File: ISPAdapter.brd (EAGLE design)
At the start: 76 x 38 mm, 10 parts, among them U1 74LVC4066PW

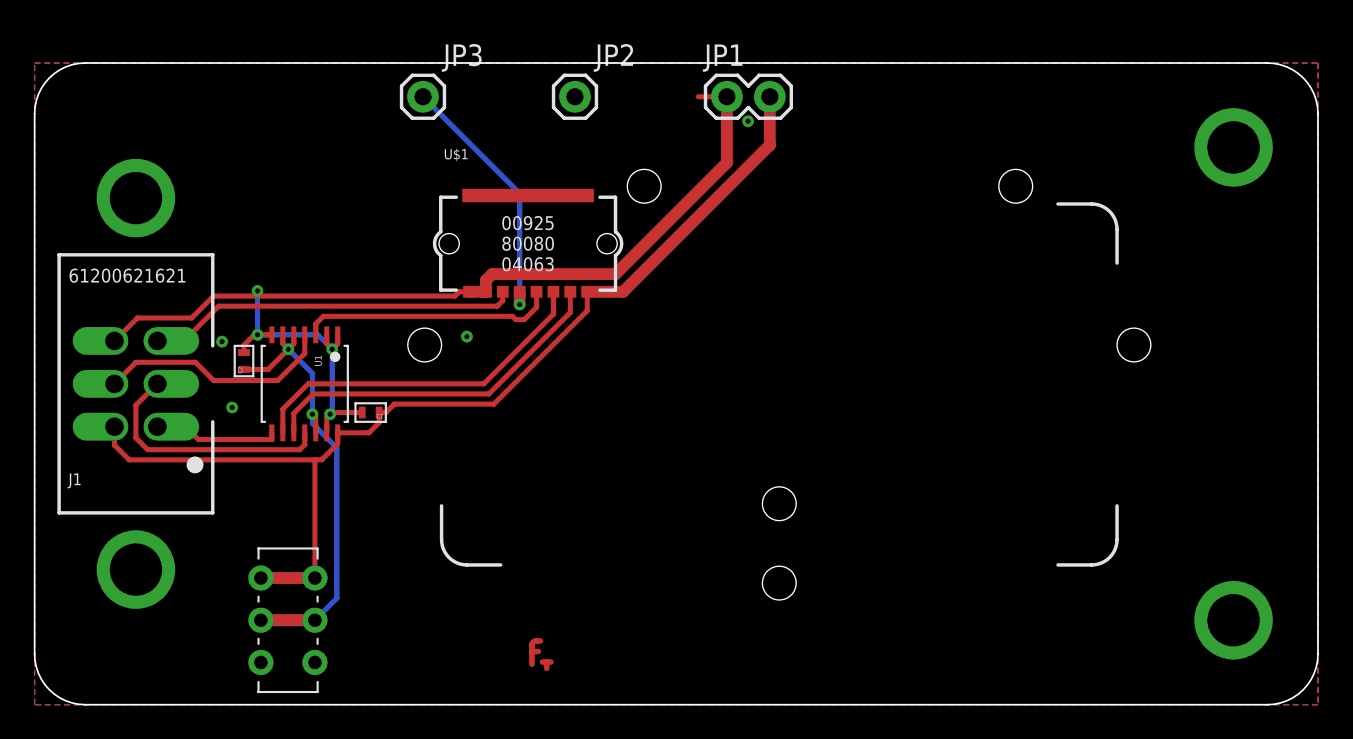
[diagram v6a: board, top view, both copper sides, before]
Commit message: Jack/Plug refs; offset pads
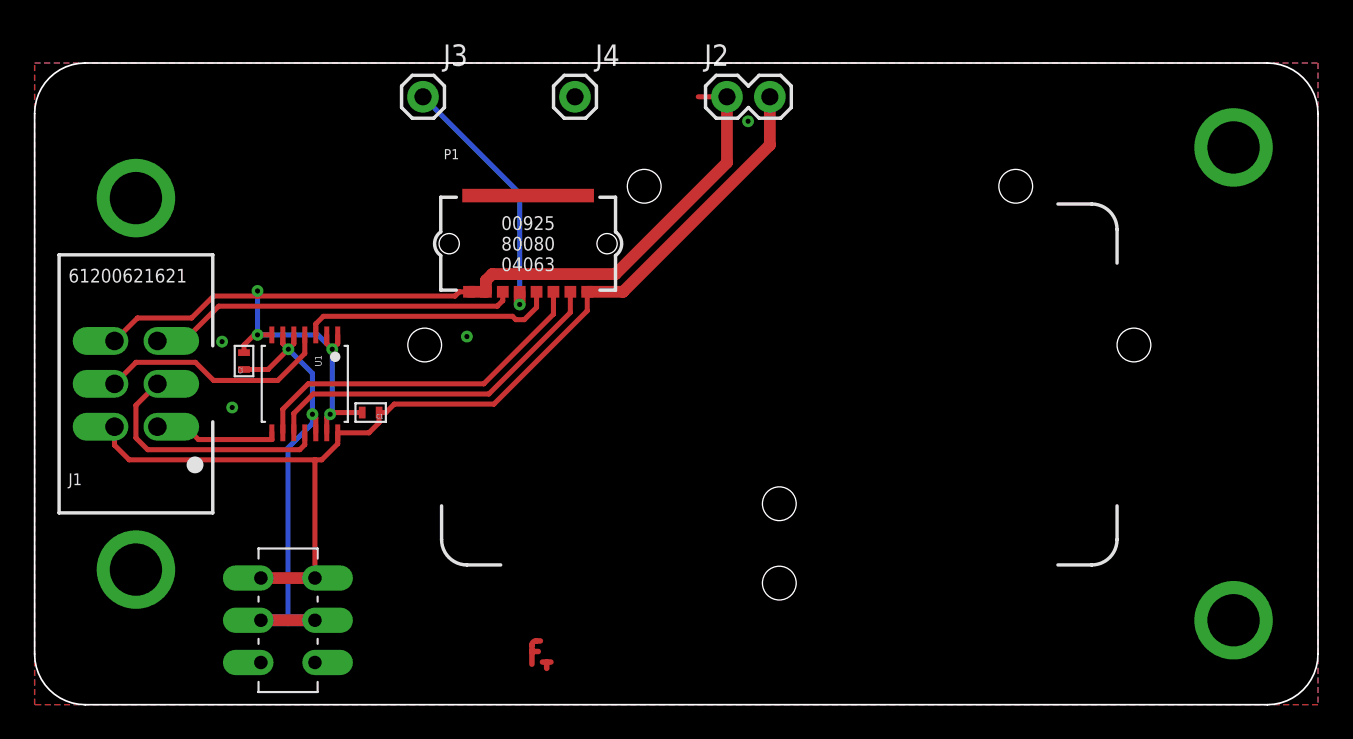
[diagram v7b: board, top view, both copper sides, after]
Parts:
- renumbered JP1 to J2, JP2 to J4, JP3 to J3, U$1 to P1
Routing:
- net VCC: track 65.6 -> 62.4 mm
- net ISP_EN: track 30.5 -> 31.4 mm
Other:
- board text added: "Rev. B (201x-xx-xx)"
- board text removed: "Rev. 2 (201x-xx-xx)"
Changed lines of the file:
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@@
 <circle x="23.1" y="21.3" radius="1.7" width="0.5" layer="107"/>
 <text x="32" y="34" size="1" layer="107" font="vector" ratio="15" rot="SR270" align="center-left">GND</text>
-<text x="38" y="23" size="0.8128" layer="107" font="vector" ratio="15" align="top-left">Rev. 2 (201x-xx-xx)</text>
+<text x="38" y="23" size="0.8128" layer="107" font="vector" ratio="15" align="top-left">Rev. B (201x-xx-xx)</text>
 <text x="23" y="34" size="1" layer="107" font="vector" ratio="15" rot="SR270" align="center-left">PB3</text>
-<text x="18" y="0.7" size="1.5" layer="107" font="vector" ratio="15">DW</text>
-<text x="18" y="9.3" size="1.5" layer="107" font="vector" ratio="15" align="top-left">SPI</text>
+<text x="19.5" y="0.7" size="1.5" layer="107" font="vector" ratio="15">DW</text>
+<text x="19.5" y="9.3" size="1.5" layer="107" font="vector" ratio="15" align="top-left">SPI</text>
 <text x="25.8" y="23.7" size="0.8128" layer="107" font="vector" ratio="15" align="top-center">6</text>
 </plain>
@@
 <attribute name="DIGIKEY_PART_#" value="732-5394-ND" x="6" y="19" size="1.778" layer="27" display="off"/>
 </element>
-<element name="JP1" library="SparkFun-Connectors" package="1X02" value="M02PTH" x="41" y="36"/>
-<element name="U$1" library="dubec" package="AVX9258-8C" value="AVX9258" x="29.225" y="27.3">
+<element name="J2" library="SparkFun-Connectors" package="1X02" value="M02PTH" x="41" y="36"/>
+<element name="P1" library="dubec" package="AVX9258-8C" value="AVX9258" x="29.225" y="27.3">
 <attribute name="MANUFACTURER" value="AVX Corporation" x="29.225" y="27.3" size="1.778" layer="27" display="off"/>
 <attribute name="EURO" value="1.30" x="29.225" y="27.3" size="1.778" layer="27" display="off"/>
@@
 <attribute name="DIGIKEY_PART_#" value="478-5495-1-ND" x="29.225" y="27.3" size="1.778" layer="27" display="off"/>
 </element>
-<element name="JP2" library="SparkFun-Connectors" package="1X01" value="M01PTH" x="32" y="36"/>
+<element name="J4" library="SparkFun-Connectors" package="1X01" value="M01PTH" x="32" y="36"/>
 <element name="U$2" library="dubec" package="TF-EMBLEM" value="" x="30" y="3"/>
-<element name="JP3" library="SparkFun-Connectors" package="1X01" value="M01PTH" x="23" y="36"/>
+<element name="J3" library="SparkFun-Connectors" package="1X01" value="M01PTH" x="23" y="36"/>
 <element name="U1" library="dubec" package="14-TSSOP" value="74LVC4066PW" x="16" y="19" rot="R270">
 <attribute name="MANUFACTURER" value="NXP Semiconductors" x="16" y="19" size="1.778" layer="27" rot="R270" display="off"/>
@@
 <signal name="VCC">
 <contactref element="J1" pad="2"/>
-<contactref element="JP1" pad="2"/>
-<contactref element="U$1" pad="1"/>
+<contactref element="J2" pad="2"/>
+<contactref element="P1" pad="1"/>
 <contactref element="U1" pad="14"/>
 <wire x1="32.725" y1="24.45" x2="34.85" y2="24.45" width="0.7" layer="1"/>
@@
 <contactref element="S1" pad="1"/>
 <contactref element="S1" pad="4"/>
-<wire x1="13.4" y1="7.5" x2="16.6" y2="7.5" width="0.7" layer="16"/>
 <wire x1="13.4" y1="7.5" x2="16.6" y2="7.5" width="0.7" layer="1"/>
 <wire x1="32.725" y1="23.325" x2="32.725" y2="24.45" width="0.3" layer="1"/>
@@
 <contactref element="U1" pad="3"/>
 <wire x1="16.65" y1="22.55" x2="16.65" y2="21.9" width="0.3" layer="1"/>
-<contactref element="U$1" pad="4"/>
+<contactref element="P1" pad="4"/>
 <wire x1="29.725" y1="24.45" x2="29.725" y2="23.525" width="0.3" layer="1"/>
 <wire x1="29.725" y1="23.525" x2="29" y2="22.8" width="0.3" layer="1"/>
@@
 <signal name="DGND">
 <contactref element="J1" pad="6"/>
-<contactref element="JP1" pad="1"/>
+<contactref element="J2" pad="1"/>
 <wire x1="27.1" y1="25.5" x2="26.725" y2="25.125" width="0.7" layer="1"/>
-<contactref element="U$1" pad="7"/>
+<contactref element="P1" pad="7"/>
 <wire x1="27.1" y1="25.5" x2="34.4" y2="25.5" width="0.7" layer="1"/>
 <wire x1="34.4" y1="25.5" x2="41" y2="32.1" width="0.7" layer="1"/>
@@
 <wire x1="26.725" y1="25.125" x2="26.725" y2="24.45" width="0.7" layer="1"/>
 <contactref element="C1" pad="2"/>
-<contactref element="U$1" pad="8"/>
+<contactref element="P1" pad="8"/>
 <wire x1="26.725" y1="24.45" x2="25.725" y2="24.45" width="0.7" layer="1"/>
 <contactref element="C2" pad="2"/>
@@
 </signal>
 <signal name="MISO">
-<contactref element="U$1" pad="3"/>
+<contactref element="P1" pad="3"/>
 <wire x1="30.725" y1="23.125" x2="26.6" y2="19" width="0.3" layer="1"/>
 <wire x1="26.6" y1="19" x2="16.2" y2="19" width="0.3" layer="1"/>
@@
 </signal>
 <signal name="SCK">
-<contactref element="U$1" pad="2"/>
+<contactref element="P1" pad="2"/>
 <wire x1="31.725" y1="23.225" x2="26.9" y2="18.4" width="0.3" layer="1"/>
 <wire x1="26.9" y1="18.4" x2="16.5" y2="18.4" width="0.3" layer="1"/>
@@
 <signal name="RESET">
 <contactref element="J1" pad="5"/>
-<contactref element="U$1" pad="6"/>
+<contactref element="P1" pad="6"/>
 <wire x1="27.725" y1="23.925" x2="27.4" y2="23.6" width="0.3" layer="1"/>
 <wire x1="27.4" y1="23.6" x2="10.9" y2="23.6" width="0.3" layer="1"/>
@@
 <via x="71" y="33" extent="1-16" drill="3.1"/>
 <via x="71" y="5" extent="1-16" drill="3.1"/>
-<contactref element="JP2" pad="1"/>
+<contactref element="J4" pad="1"/>
 <wire x1="39.3" y1="36" x2="41.1" y2="36" width="0.3" layer="1"/>
 <polygon width="0.254" layer="16">
@@
 </signal>
 <signal name="AUX">
-<contactref element="JP3" pad="1"/>
+<contactref element="J3" pad="1"/>
 <via x="28.725" y="23.7" extent="1-16" drill="0.3"/>
-<contactref element="U$1" pad="5"/>
+<contactref element="P1" pad="5"/>
 <wire x1="28.725" y1="24.45" x2="28.725" y2="23.7" width="0.7" layer="1"/>
 <wire x1="28.725" y1="23.7" x2="28.725" y2="30.275" width="0.3" layer="16"/>
@@
 <contactref element="S1" pad="2"/>
 <contactref element="S1" pad="5"/>
-<wire x1="16.6" y1="5" x2="13.4" y2="5" width="0.7" layer="16"/>
+<wire x1="16.6" y1="5" x2="15" y2="5" width="0.7" layer="16"/>
+<wire x1="15" y1="5" x2="13.4" y2="5" width="0.7" layer="16"/>
 <wire x1="13.4" y1="5" x2="16.6" y2="5" width="0.7" layer="1"/>
 <contactref element="U1" pad="12"/>
@@
 <wire x1="12.4" y1="19.85" x2="13.825" y2="19.85" width="0.3" layer="1"/>
 <wire x1="13.825" y1="19.85" x2="15.025" y2="21.05" width="0.3" layer="1"/>
-<wire x1="16.6" y1="5" x2="17.9" y2="6.3" width="0.3" layer="16"/>
-<wire x1="17.9" y1="6.3" x2="17.9" y2="15.2" width="0.3" layer="16"/>
 <wire x1="16.65" y1="16.1" x2="16.65" y2="17" width="0.3" layer="1"/>
 <wire x1="16.65" y1="17" x2="16.45" y2="17.2" width="0.3" layer="1"/>
-<wire x1="17.9" y1="15.2" x2="16.45" y2="16.65" width="0.3" layer="16"/>
 <wire x1="16.45" y1="16.65" x2="16.45" y2="17.2" width="0.3" layer="16"/>
 <wire x1="16.45" y1="17.2" x2="16.45" y2="19.625" width="0.3" layer="16"/>
 <wire x1="16.45" y1="19.625" x2="15.025" y2="21.05" width="0.3" layer="16"/>
+<wire x1="18.1" y1="5" x2="16.6" y2="5" width="0.3" layer="16"/>
+<wire x1="16.45" y1="16.65" x2="15" y2="15.2" width="0.3" layer="16"/>
+<wire x1="15" y1="15.2" x2="15" y2="5" width="0.3" layer="16"/>
 </signal>
 <signal name="SCK_PROG">

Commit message: Tweaks
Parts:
- moved S1 1.00 mm to (15.0, 6.00)
- moved C1 0.64 mm to (19.4, 17.7), turned to 90 degrees
- moved C2 0.20 mm to (12.6, 20.4)
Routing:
- net ISP_EN: track 31.4 -> 28.7 mm
- net VCC: track 62.4 -> 61.6 mm
- net DGND: track 64.0 -> 64.5 mm
- net GND: vias 8 -> 9
